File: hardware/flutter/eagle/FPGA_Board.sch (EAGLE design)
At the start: 81 parts, among them IC1 AT45DB161D-SU, IC2 MEGA8-AI, IC3 MAX481CSA, Q1 8Mhz, U2 XC3S50AVQ100, X1 BU-SMA-V, X2 MINI-USB-32005-201

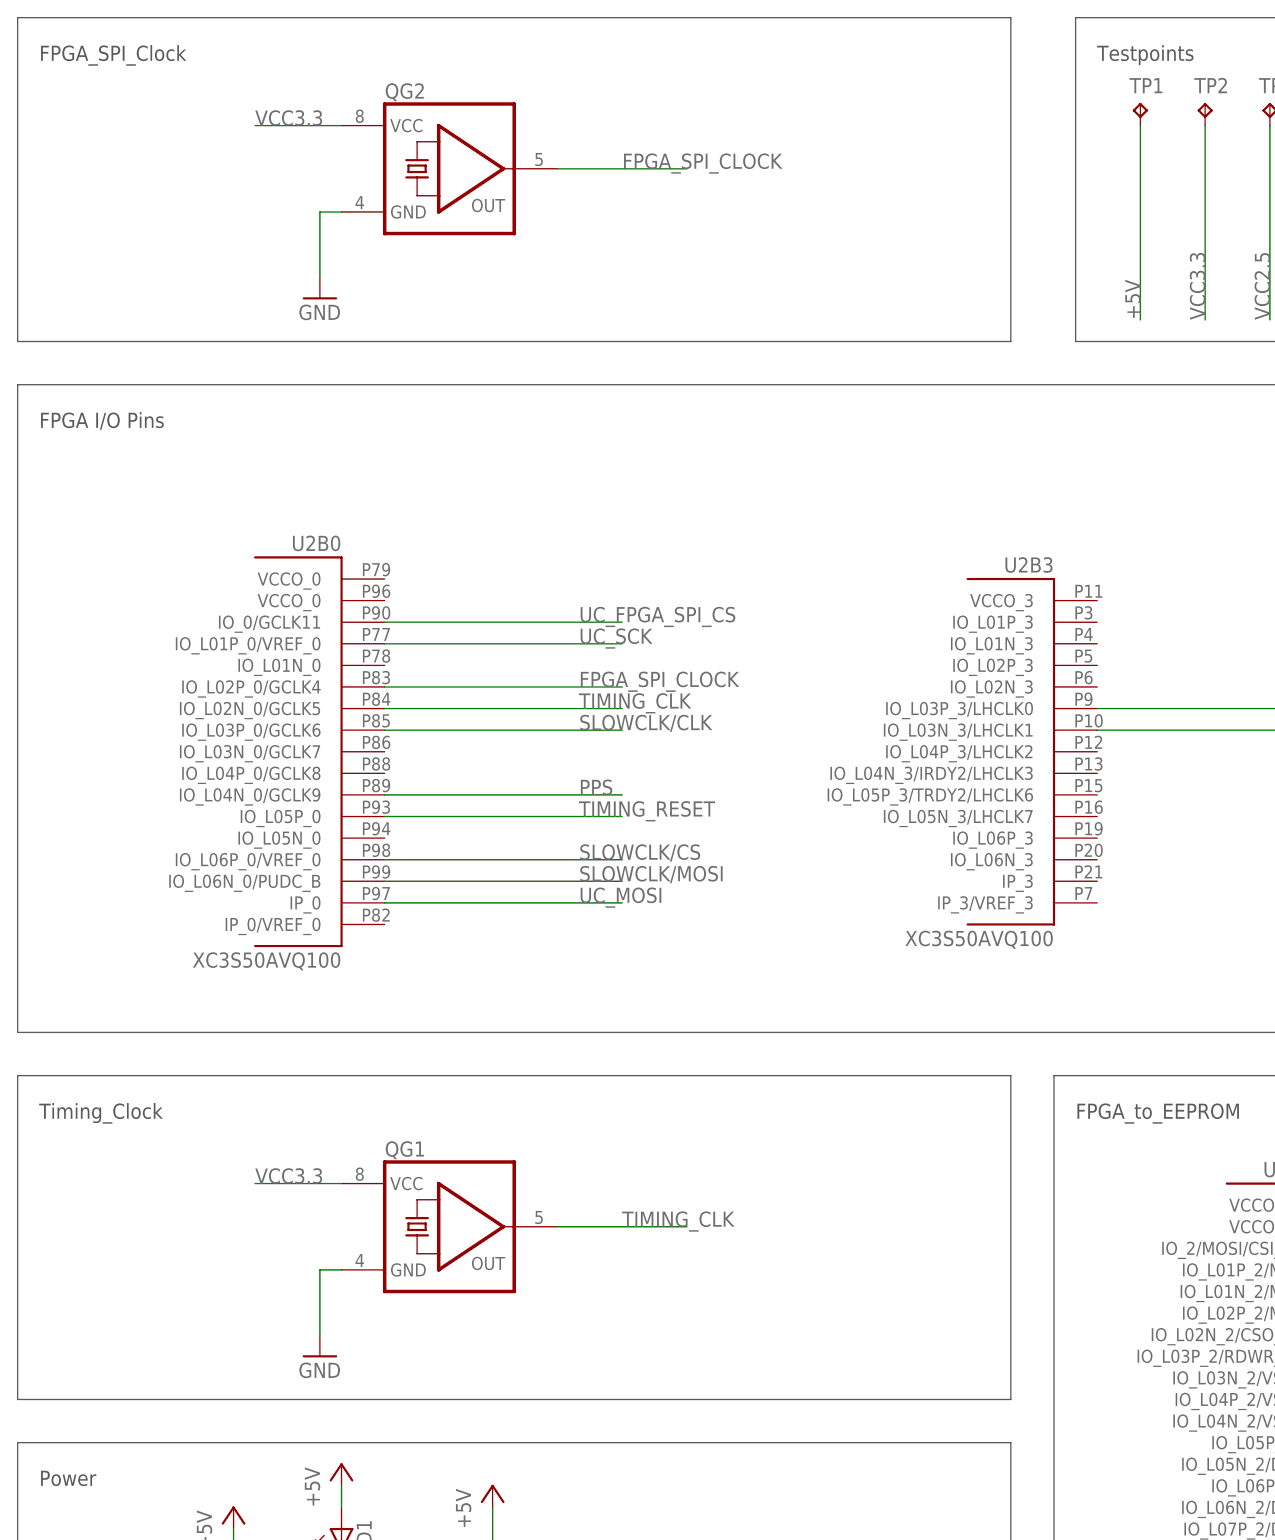
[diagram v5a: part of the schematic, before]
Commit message: added alternative pads for an oscillator with other pinlayout in flutter0 layout of oscillator was added to hgg.lbr
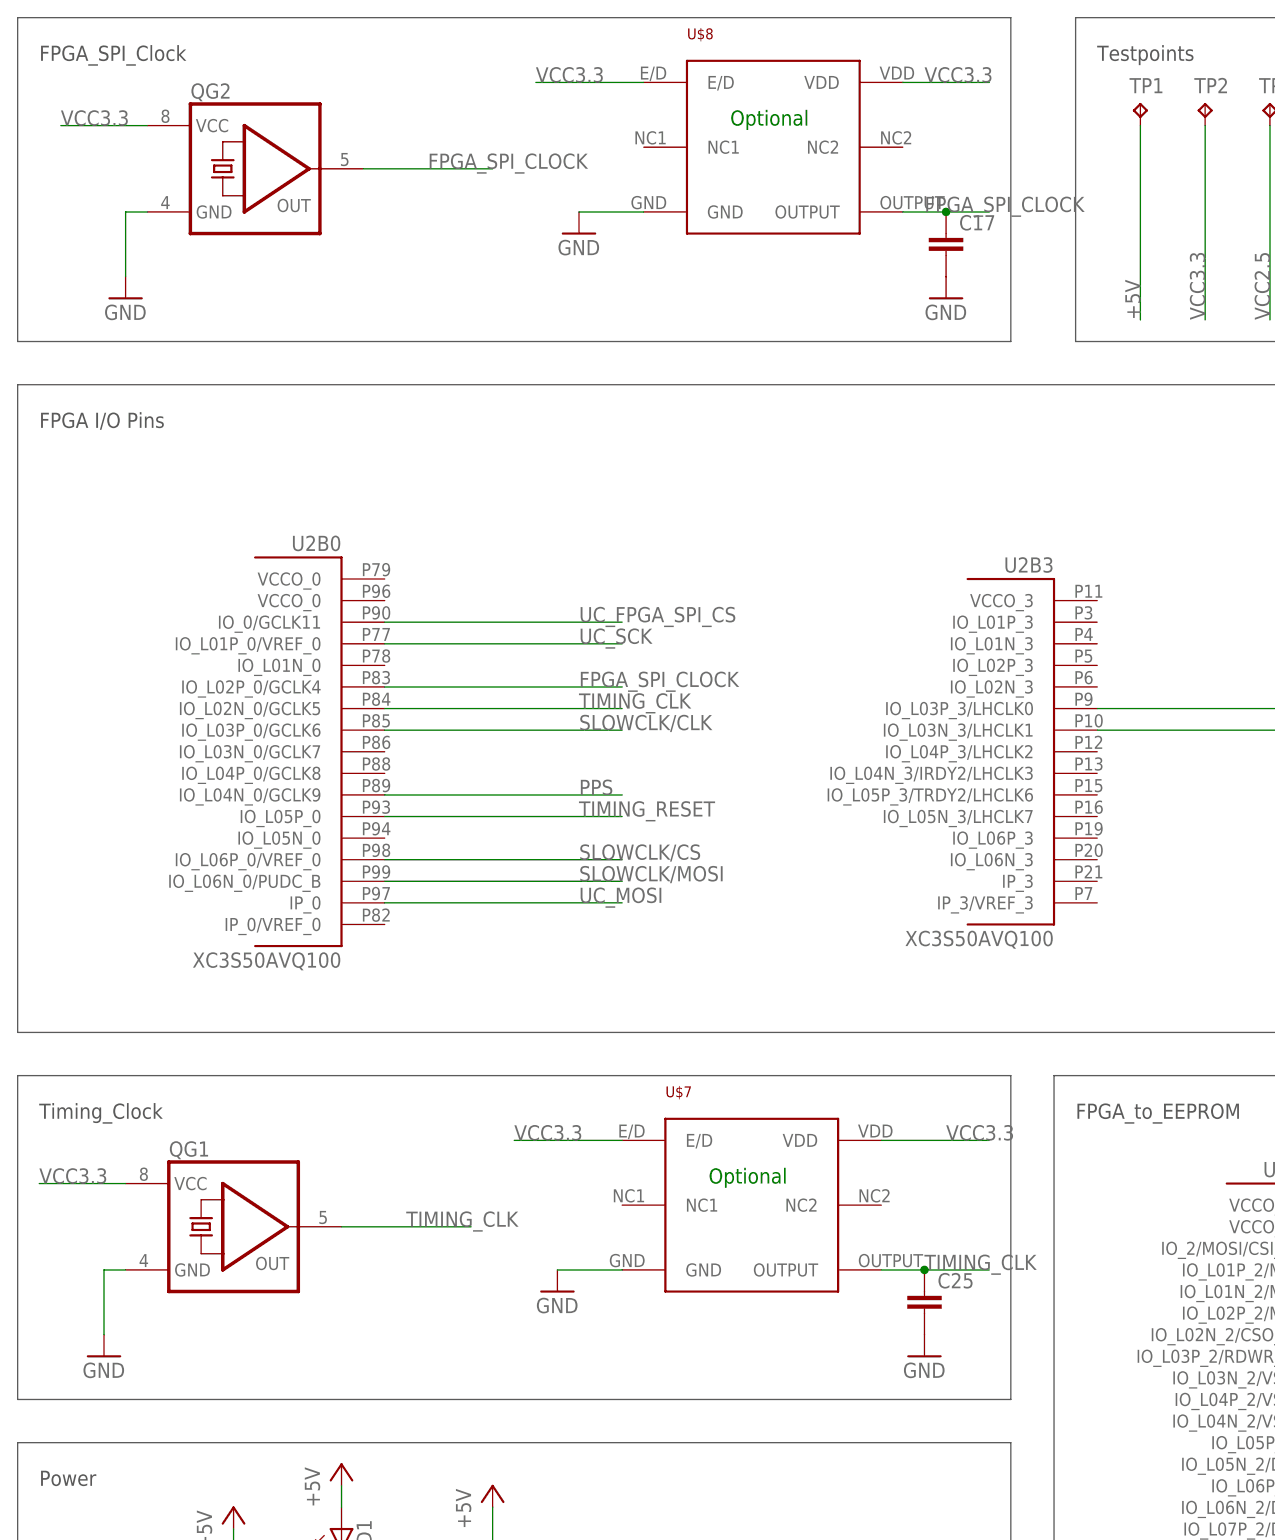
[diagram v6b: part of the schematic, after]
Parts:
- added C17, C25: (no value), resistor:C-EUC0603
- added U$7, U$8: OSCILLATOR, hgg:OSCILLATOR
- Q1: device crystal:CRYSTALHC49UP -> crystal:CRYSTALSM49
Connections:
- net FPGA_SPI_CLOCK: now also C17.1, U$8.OUTPUT
- net GND: now also C17.2, C25.2, U$7.GND, U$8.GND
- net TIMING_CLK: now also C25.1, U$7.OUTPUT
- net VCC3.3: now also U$7.E/D, U$7.VDD, U$8.E/D, U$8.VDD
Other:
- note added: "Optional"
- moved on the sheet: QG1, QG2
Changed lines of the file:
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@@
 <part name="GND25" library="supply1" deviceset="GND" device=""/>
 <part name="GND27" library="supply1" deviceset="GND" device=""/>
-<part name="Q1" library="crystal" deviceset="CRYSTAL" device="HC49UP" value="8Mhz"/>
+<part name="Q1" library="crystal" deviceset="CRYSTAL" device="SM49" value="8Mhz"/>
 <part name="C11" library="resistor" deviceset="C-EU" device="C0805" value="22n"/>
 <part name="C12" library="resistor" deviceset="C-EU" device="C0805" value="22n"/>
@@
 <part name="JP4" library="pinhead" deviceset="PINHD-2X5" device="" value="ISP"/>
 <part name="GND26" library="supply1" deviceset="GND" device=""/>
+<part name="U$7" library="hgg" deviceset="OSCILLATOR" device=""/>
+<part name="U$8" library="hgg" deviceset="OSCILLATOR" device=""/>
+<part name="GND48" library="supply1" deviceset="GND" device=""/>
+<part name="GND49" library="supply1" deviceset="GND" device=""/>
+<part name="C17" library="resistor" deviceset="C-EU" device="C0603"/>
+<part name="C25" library="resistor" deviceset="C-EU" device="C0603"/>
+<part name="GND50" library="supply1" deviceset="GND" device=""/>
+<part name="GND51" library="supply1" deviceset="GND" device=""/>
 </parts>
 <sheets>
@@
 <wire x1="269.24" y1="355.6" x2="269.24" y2="317.5" width="0.1524" layer="97"/>
 <text x="127" y="350.52" size="1.778" layer="97">Testpoints</text>
+<text x="83.82" y="342.9" size="1.778" layer="91">Optional</text>
+<text x="81.28" y="218.44" size="1.778" layer="91">Optional</text>
 </plain>
 <instances>
@@
 <instance part="U$4" gate="G$1" x="182.88" y="104.14"/>
 <instance part="IC1" gate="G$1" x="271.78" y="154.94"/>
-<instance part="QG1" gate="1" x="50.8" y="213.36"/>
-<instance part="GND16" gate="1" x="35.56" y="198.12"/>
+<instance part="QG1" gate="1" x="25.4" y="213.36"/>
+<instance part="GND16" gate="1" x="10.16" y="198.12"/>
 <instance part="GND17" gate="1" x="289.56" y="144.78"/>
 <instance part="R13" gate="G$1" x="241.3" y="182.88" rot="R90"/>
@@
 <instance part="R18" gate="G$1" x="452.12" y="200.66" rot="R90"/>
 <instance part="GND32" gate="1" x="452.12" y="193.04"/>
-<instance part="QG2" gate="1" x="50.8" y="337.82"/>
-<instance part="GND33" gate="1" x="35.56" y="322.58"/>
+<instance part="QG2" gate="1" x="27.94" y="337.82"/>
+<instance part="GND33" gate="1" x="12.7" y="322.58"/>
 <instance part="R19" gate="G$1" x="441.96" y="198.12" rot="R90"/>
 <instance part="GND34" gate="1" x="441.96" y="190.5"/>
@@
 <instance part="JP4" gate="A" x="271.78" y="208.28"/>
 <instance part="GND26" gate="1" x="299.72" y="187.96"/>
+<instance part="U$7" gate="G$1" x="86.36" y="215.9"/>
+<instance part="U$8" gate="G$1" x="88.9" y="340.36"/>
+<instance part="GND48" gate="1" x="63.5" y="205.74"/>
+<instance part="GND49" gate="1" x="66.04" y="330.2"/>
+<instance part="C17" gate="G$1" x="109.22" y="330.2"/>
+<instance part="C25" gate="G$1" x="106.68" y="205.74"/>
+<instance part="GND50" gate="1" x="106.68" y="198.12"/>
+<instance part="GND51" gate="1" x="109.22" y="322.58"/>
 </instances>
 <busses>
@@
 <pinref part="QG1" gate="1" pin="GND"/>
 <pinref part="GND16" gate="1" pin="GND"/>
-<wire x1="38.1" y1="208.28" x2="35.56" y2="208.28" width="0.1524" layer="91"/>
-<wire x1="35.56" y1="208.28" x2="35.56" y2="200.66" width="0.1524" layer="91"/>
+<wire x1="12.7" y1="208.28" x2="10.16" y2="208.28" width="0.1524" layer="91"/>
+<wire x1="10.16" y1="208.28" x2="10.16" y2="200.66" width="0.1524" layer="91"/>
 </segment>
 <segment>
@@
 <pinref part="QG2" gate="1" pin="GND"/>
 <pinref part="GND33" gate="1" pin="GND"/>
-<wire x1="38.1" y1="332.74" x2="35.56" y2="332.74" width="0.1524" layer="91"/>
-<wire x1="35.56" y1="332.74" x2="35.56" y2="325.12" width="0.1524" layer="91"/>
+<wire x1="15.24" y1="332.74" x2="12.7" y2="332.74" width="0.1524" layer="91"/>
+<wire x1="12.7" y1="332.74" x2="12.7" y2="325.12" width="0.1524" layer="91"/>
 </segment>
 <segment>
@@
 <wire x1="299.72" y1="203.2" x2="299.72" y2="190.5" width="0.1524" layer="91"/>
 <pinref part="GND26" gate="1" pin="GND"/>
+</segment>
+<segment>
+<pinref part="U$7" gate="G$1" pin="GND"/>
+<wire x1="71.12" y1="208.28" x2="63.5" y2="208.28" width="0.1524" layer="91"/>
+<pinref part="GND48" gate="1" pin="GND"/>
+</segment>
+<segment>
+<pinref part="GND49" gate="1" pin="GND"/>
+<pinref part="U$8" gate="G$1" pin="GND"/>
+<wire x1="66.04" y1="332.74" x2="73.66" y2="332.74" width="0.1524" layer="91"/>
+</segment>
+<segment>
+<pinref part="C25" gate="G$1" pin="2"/>
+<pinref part="GND50" gate="1" pin="GND"/>
+</segment>
+<segment>
+<pinref part="C17" gate="G$1" pin="2"/>
+<pinref part="GND51" gate="1" pin="GND"/>
 </segment>
 </net>
@@
 <segment>
 <pinref part="QG1" gate="1" pin="VCC"/>
-<wire x1="38.1" y1="218.44" x2="27.94" y2="218.44" width="0.1524" layer="91"/>
-<label x="27.94" y="218.44" size="1.778" layer="95"/>
+<wire x1="12.7" y1="218.44" x2="2.54" y2="218.44" width="0.1524" layer="91"/>
+<label x="2.54" y="218.44" size="1.778" layer="95"/>
 </segment>
 <segment>
@@
 <segment>
 <pinref part="QG2" gate="1" pin="VCC"/>
-<wire x1="38.1" y1="342.9" x2="27.94" y2="342.9" width="0.1524" layer="91"/>
-<label x="27.94" y="342.9" size="1.778" layer="95"/>
+<wire x1="15.24" y1="342.9" x2="5.08" y2="342.9" width="0.1524" layer="91"/>
+<label x="5.08" y="342.9" size="1.778" layer="95"/>
 </segment>
 <segment>
@@
 <wire x1="276.86" y1="213.36" x2="299.72" y2="213.36" width="0.1524" layer="91"/>
 <label x="297.18" y="213.36" size="1.778" layer="95"/>
+</segment>
+<segment>
+<pinref part="U$7" gate="G$1" pin="E/D"/>
+<wire x1="71.12" y1="223.52" x2="58.42" y2="223.52" width="0.1524" layer="91"/>
+<label x="58.42" y="223.52" size="1.778" layer="95"/>
+</segment>
+<segment>
+<pinref part="U$7" gate="G$1" pin="VDD"/>
+<wire x1="101.6" y1="223.52" x2="114.3" y2="223.52" width="0.1524" layer="91"/>
+<label x="109.22" y="223.52" size="1.778" layer="95"/>
+</segment>
+<segment>
+<pinref part="U$8" gate="G$1" pin="E/D"/>
+<wire x1="73.66" y1="347.98" x2="60.96" y2="347.98" width="0.1524" layer="91"/>
+<label x="60.96" y="347.98" size="1.778" layer="95"/>
+</segment>
+<segment>
+<pinref part="U$8" gate="G$1" pin="VDD"/>
+<wire x1="104.14" y1="347.98" x2="114.3" y2="347.98" width="0.1524" layer="91"/>
+<label x="106.68" y="347.98" size="1.778" layer="95"/>
 </segment>
 </net>
@@
 <segment>
 <pinref part="QG2" gate="1" pin="OUT"/>
-<wire x1="63.5" y1="337.82" x2="78.74" y2="337.82" width="0.1524" layer="91"/>
-<label x="71.12" y="337.82" size="1.778" layer="95"/>
+<wire x1="40.64" y1="337.82" x2="55.88" y2="337.82" width="0.1524" layer="91"/>
+<label x="48.26" y="337.82" size="1.778" layer="95"/>
 </segment>
 <segment>
@@
 <wire x1="193.04" y1="342.9" x2="193.04" y2="320.04" width="0.1524" layer="91"/>
 <label x="193.04" y="320.04" size="1.778" layer="95" rot="R90"/>
+</segment>
+<segment>
+<pinref part="U$8" gate="G$1" pin="OUTPUT"/>
+<wire x1="104.14" y1="332.74" x2="109.22" y2="332.74" width="0.1524" layer="91"/>
+<label x="106.68" y="332.74" size="1.778" layer="95"/>
+<pinref part="C17" gate="G$1" pin="1"/>
+<wire x1="109.22" y1="332.74" x2="114.3" y2="332.74" width="0.1524" layer="91"/>
+<junction x="109.22" y="332.74"/>
 </segment>
 </net>
@@
 <segment>
 <pinref part="QG1" gate="1" pin="OUT"/>
-<wire x1="63.5" y1="213.36" x2="78.74" y2="213.36" width="0.1524" layer="91"/>
-<label x="71.12" y="213.36" size="1.778" layer="95"/>
+<wire x1="38.1" y1="213.36" x2="53.34" y2="213.36" width="0.1524" layer="91"/>
+<label x="45.72" y="213.36" size="1.778" layer="95"/>
 </segment>
 <segment>
@@
 <label x="185.42" y="320.04" size="1.778" layer="95" rot="R90"/>
 </segment>
-</net>
+<segment>
+<pinref part="U$7" gate="G$1" pin="OUTPUT"/>
+<wire x1="101.6" y1="208.28" x2="106.68" y2="208.28" width="0.1524" layer="91"/>
+<label x="106.68" y="208.28" size="1.778" layer="95"/>
+<pinref part="C25" gate="G$1" pin="1"/>
+<wire x1="106.68" y1="208.28" x2="114.3" y2="208.28" width="0.1524" layer="91"/>
+<junction x="106.68" y="208.28"/>
+</segment>
+</net>
